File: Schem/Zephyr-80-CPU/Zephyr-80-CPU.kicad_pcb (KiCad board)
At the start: 6 copper layers, 160 x 64.4 mm, 62 parts, among them J1 pBITzBus, SW1 SW_Coded_SH-7070, SW2 SW_Coded_SH-7070, SW3 SW_Coded_SH-7070, SW4 SW_Coded_SH-7070, SW5 SW_Coded_SH-7070, SW6 SW_Coded_SH-7070, SW7 SW_Coded_SH-7070, U1 AS7C4096A-12TCN, U10 74HC244, U11 74HC244, U12 74HC138, U2 ATF22V10C-10PU, U3 Z084000xP, U4 SST39SF040-70-4C-PHE, U5 ATF22V10C-10PU, U6 SN74HC273DWR, U7 SN74HC244DWR, U8 74HC244, U9 74HC244, Y1 ECS-2100AX-100

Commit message: Routed the CPU board. Removed the rotary switches decoder
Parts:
- removed C10, C11, C12, C13, C9: 100n, Capacitor_SMD:C_0603_1608Metric
- removed R1, R10, R11, R12, R13, R14, R15, R16, R17, R18, R19, R2, R20, R21, R22, R23, R24, R25, R26, R27, R28, R3, R4, R5, R6, R7, R8, R9: 4k7, Resistor_SMD:R_0603_1608Metric
- removed SW1, SW2, SW3, SW4, SW5, SW6, SW7: SW_Coded_SH-7070, Button_Switch_THT:Nidec_Copal_SH-7010C
- removed U10, U11, U8, U9: 74HC244, Package_SO:TSSOP-20_4.4x6.5mm_P0.65mm
- removed U12: 74HC138, Package_SO:SSOP-16_5.3x6.2mm_P0.65mm
- moved U7 382.2 mm to (187.5, 78.0), turned to 0 degrees
- moved C3 380.6 mm to (153.1, 53.0), turned to 0 degrees
- moved C1 378.4 mm to (149.2, 53.0), turned to 180 degrees
- moved U6 376.2 mm to (187.5, 61.2), turned to 0 degrees
- moved C8 360.4 mm to (192.6, 69.6)
- moved C2 352.3 mm to (178.9, 53.1), turned to 180 degrees
- moved C4 345.5 mm to (192.1, 53.5), turned to 180 degrees
- moved C7 341.5 mm to (214.4, 87.5), turned to -90 degrees
- moved C5 328.9 mm to (212.3, 54.7), turned to 0 degrees
- moved C6 323.7 mm to (230.2, 87.4)
- moved U1 45.1 mm to (222.2, 87.0)
- moved U4 34.5 mm to (195.5, 56.9)
- moved U3 32.9 mm to (152.9, 55.8)
- moved Y1 24.1 mm to (133.2, 61.0)
- moved U5 20.9 mm to (171.5, 55.8)
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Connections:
- J1 pad A21: /Device Select Decode/~{CS2} -> /CPU and Address Decoding/CS_SEL2
- J1 pad A22: /Device Select Decode/~{CS3} -> unconnected-(J1A-CS3-PadA22)
- J1 pad B21: /Device Select Decode/~{CS0} -> /CPU and Address Decoding/CS_SEL0
- J1 pad B22: /Device Select Decode/~{CS1} -> /CPU and Address Decoding/CS_SEL1
- U1 pad 10: /CPU and Address Decoding/D1 -> /CPU and Address Decoding/D2
- U1 pad 13: /CPU and Address Decoding/D2 -> /CPU and Address Decoding/D0
- U1 pad 14: /CPU and Address Decoding/D3 -> /CPU and Address Decoding/D1
- U1 pad 3: /CPU and Address Decoding/A0 -> /CPU and Address Decoding/A1
- U1 pad 36: /CPU and Address Decoding/D7 -> /CPU and Address Decoding/D3
- U1 pad 4: /CPU and Address Decoding/A1 -> /CPU and Address Decoding/A0
- U1 pad 9: /CPU and Address Decoding/D0 -> /CPU and Address Decoding/D7
- U2 pad 16: /CPU and Address Decoding/~{IO_EN} -> unconnected-(U2-IO16-Pad16)
- U2 pad 7: /CPU and Address Decoding/~{RD} -> /CPU and Address Decoding/~{WR}
- U2 pad 8: /CPU and Address Decoding/~{WR} -> /CPU and Address Decoding/~{RD}
- U5 pad 1: /CPU and Address Decoding/A15 -> /CPU and Address Decoding/A13
- U5 pad 10: /CPU and Address Decoding/~{WR} -> /CPU and Address Decoding/~{RD}
- U5 pad 3: /CPU and Address Decoding/A13 -> /CPU and Address Decoding/A15
- U5 pad 9: /CPU and Address Decoding/~{RD} -> /CPU and Address Decoding/~{WR}
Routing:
- net /CPU and Address Decoding/A7: track 9.15 -> 202.8 mm, vias 0 -> 7
- net /CPU and Address Decoding/~{RD}: track 13.8 -> 197.4 mm, vias 0 -> 3
- net /CPU and Address Decoding/A8: track 0.00 -> 169.6 mm, vias 0 -> 6
- net /CPU and Address Decoding/A6: track 9.15 -> 176.6 mm, vias 0 -> 5
- net /CPU and Address Decoding/~{WR}: track 48.5 -> 215.5 mm, vias 1 -> 4
- net /CPU and Address Decoding/A5: track 9.15 -> 170.5 mm, vias 0 -> 5
- net /CPU and Address Decoding/A9: track 0.00 -> 160.8 mm, vias 0 -> 6
- net /CPU and Address Decoding/A10: track 0.00 -> 154.6 mm, vias 0 -> 5
- net /CPU and Address Decoding/A12: track 44.6 -> 188.7 mm, vias 1 -> 4
- net /CPU and Address Decoding/A4: track 9.15 -> 147.8 mm, vias 0 -> 5
- net GND: track 0.00 -> 133.3 mm, vias 0 -> 18
- net /CPU and Address Decoding/A2: track 0.00 -> 105.7 mm, vias 0 -> 5
- net /CPU and Address Decoding/A3: track 0.00 -> 105.2 mm, vias 0 -> 4
- net /CPU and Address Decoding/~{RESET}: track 16.8 -> 121.0 mm, vias 0 -> 4
- net /CPU and Address Decoding/A11: track 75.7 -> 175.8 mm, vias 1 -> 5
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- added copper zone on In2.Cu, net +5V
- added copper zone on In1.Cu, net GND

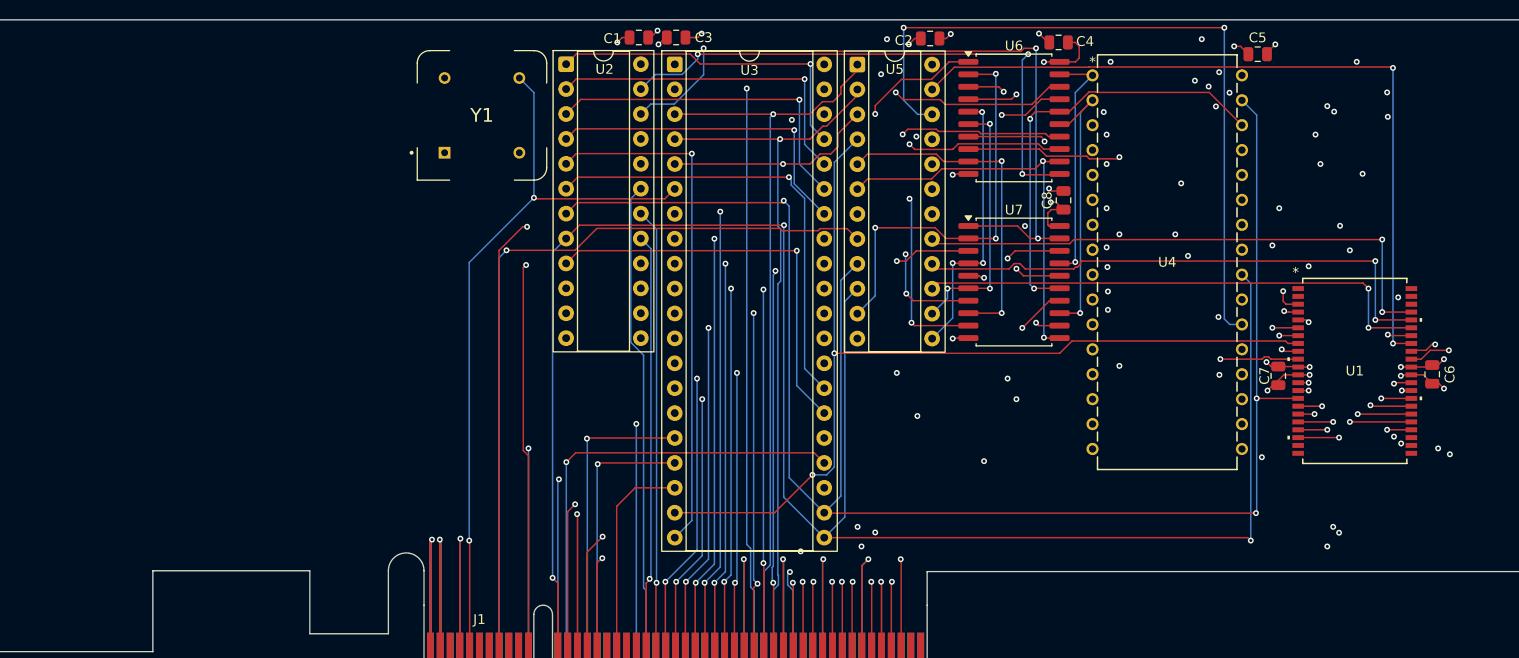
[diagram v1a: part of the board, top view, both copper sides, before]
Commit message: Added all the manufacturer part numbers to the KiCad schematics and PCB files. This will make it easier to order the parts for the project and ensure that the correct components are used. I also removed some of the old schematics that were no longer needed, such as the BaudClock, ConsolePort, DeviceSelectDecode, GPIOUserSerial, IO Controller, UserPorts, Video, and Z80HomeBrew schematics. These changes will help to streamline the design and make it easier to understand.
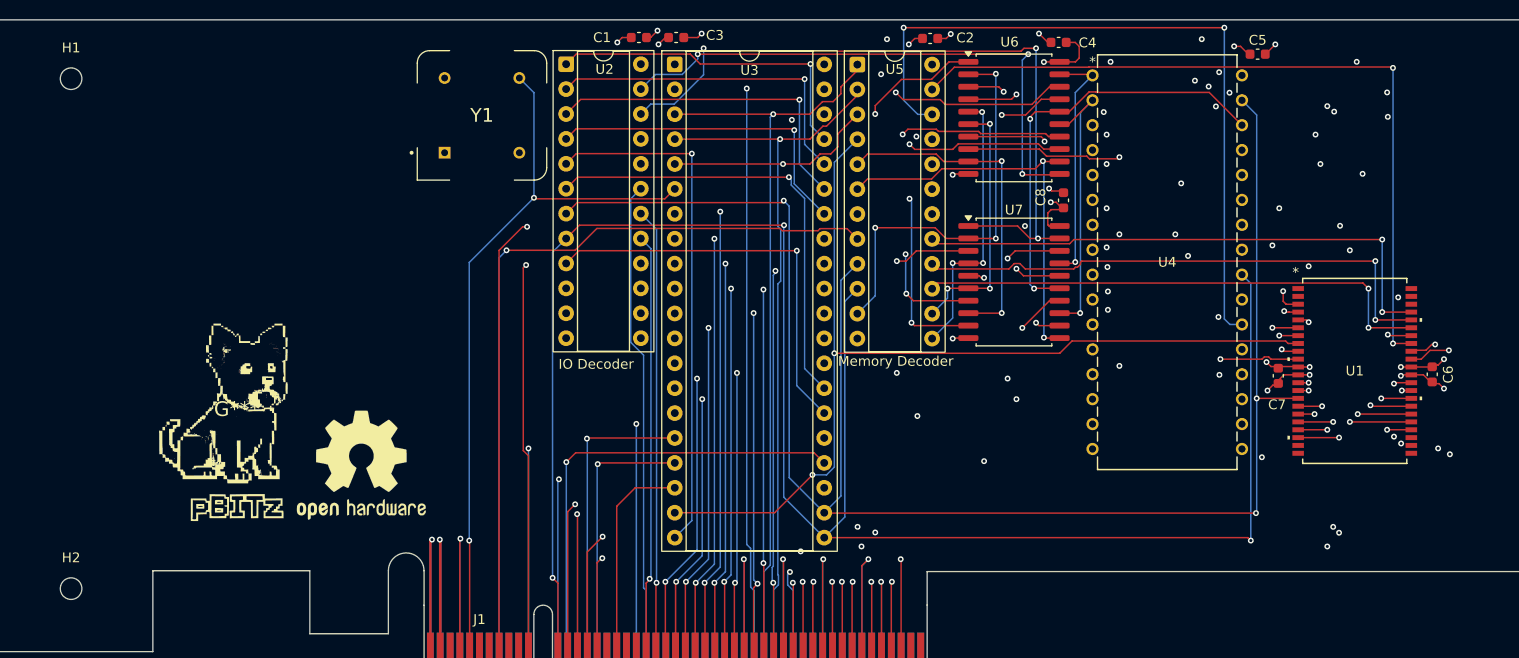
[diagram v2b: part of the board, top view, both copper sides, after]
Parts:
- added G***: LOGO, Footprints:pBITzlogo-Silk, F.Cu at (108.2, 90.9)
- added H1: MountingHole, MountingHole:MountingHole_2.2mm_M2, F.Cu at (91.3, 57.2)
- added H2: MountingHole, MountingHole:MountingHole_2.2mm_M2, F.Cu at (91.3, 109.2)
- added REF**: OSHW-Logo2_14.6x12mm_SilkScreen, Symbol:OSHW-Logo2_14.6x12mm_SilkScreen, F.Cu at (121.0, 96.6)
- C1, C2, C3, C4, C5, C6, C7, C8: footprint Capacitor_SMD:C_0805_2012Metric -> Capacitor_SMD:C_0603_1608Metric
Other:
- board text added: "IO Decoder"
- board text added: "Memory Decoder"

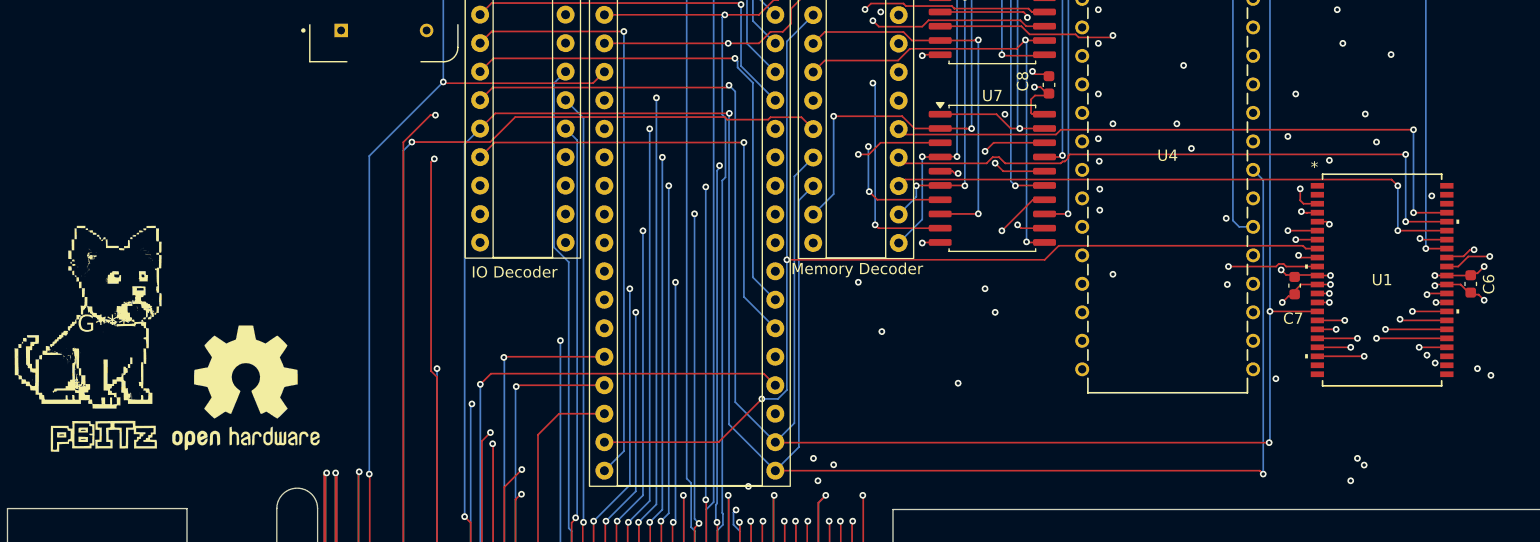
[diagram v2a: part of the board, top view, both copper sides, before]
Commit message: Fixed memory select wiring and added bulk cap on the power input.
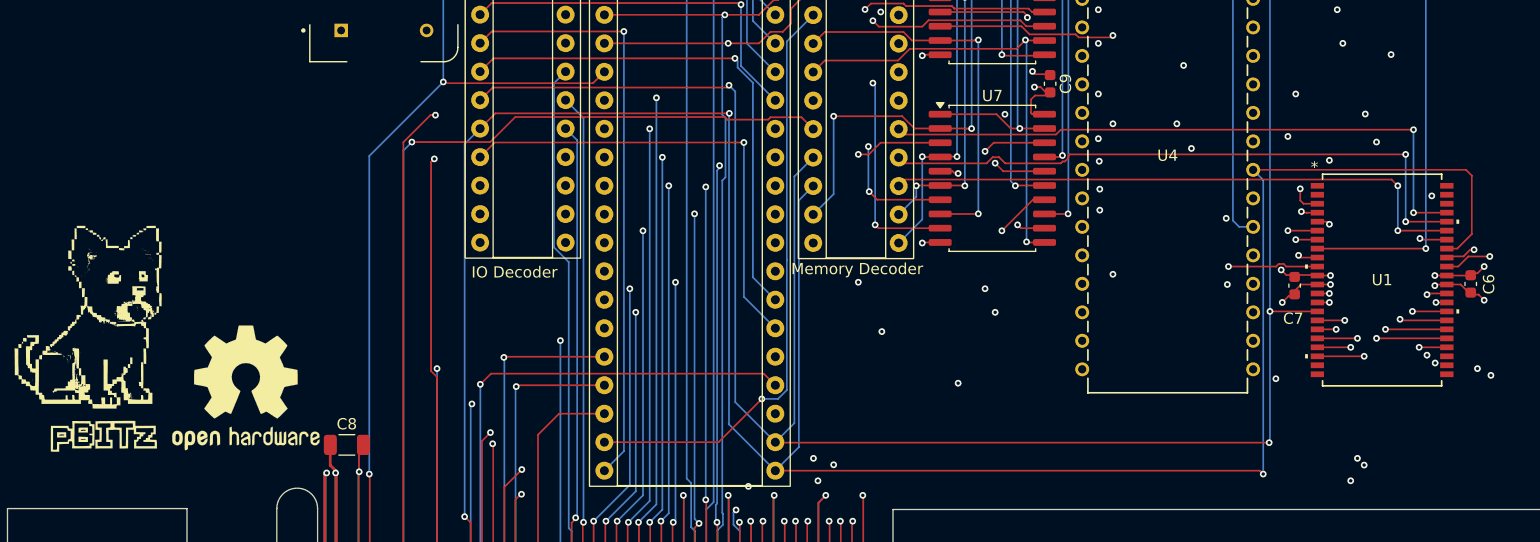
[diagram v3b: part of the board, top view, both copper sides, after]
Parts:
- added C9: 100n, Capacitor_SMD:C_0603_1608Metric, F.Cu at (192.7, 69.5)
- C8: value 100n -> 47u; footprint Capacitor_SMD:C_0603_1608Metric -> Capacitor_SMD:C_1206_3216Metric
- moved C8 70.4 mm to (129.9, 101.7), turned to 0 degrees
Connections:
- U1 pad 37: /CPU and Address Decoding/~{SRAM_CS} -> /CPU and Address Decoding/~{RD}
- U1 pad 8: /CPU and Address Decoding/~{MREQ} -> /CPU and Address Decoding/~{SRAM_CS}
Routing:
- net /CPU and Address Decoding/~{MREQ}: track 124.8 -> 76.9 mm, vias 3 -> 2
- net /CPU and Address Decoding/~{RD}: track 197.4 -> 225.1 mm
- net /CPU and Address Decoding/~{SRAM_CS}: track 78.0 -> 85.8 mm
- net +5V: track 73.4 -> 76.5 mm
- net GND: track 133.3 -> 135.8 mm

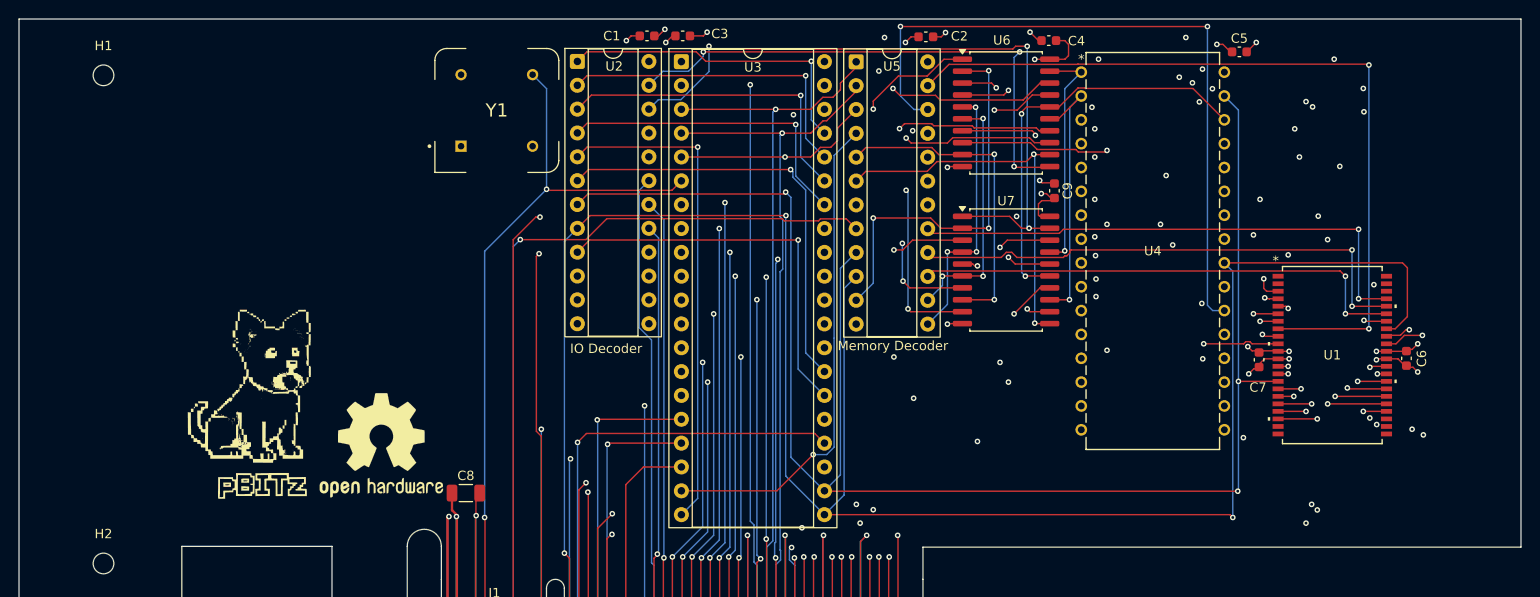
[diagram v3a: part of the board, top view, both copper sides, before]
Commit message: Added copper pours on top and bottom layers of IO controller board, and added a few vias to connect them. This should help with heat dissipation and EMI shielding.
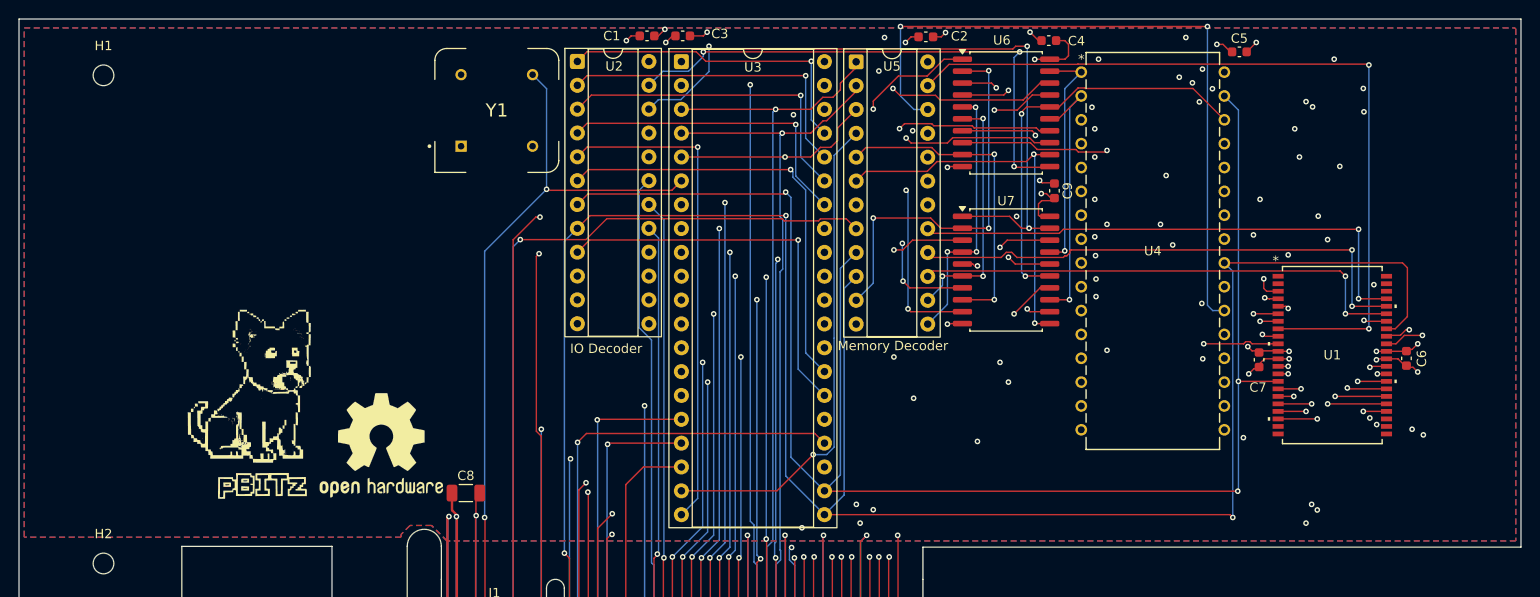
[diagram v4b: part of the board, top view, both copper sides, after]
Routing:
- added copper zone on B.Cu, net GND
- added copper zone on F.Cu, net GND
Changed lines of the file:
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@@
+		(net 1)
+		(net_name "GND")
+		(layers "F.Cu" "B.Cu")
+		(hatch edge 0.5)
+		(priority 2)
+		(connect_pads no
+			(clearance 0.4)
+		)
+		(min_thickness 0.127)
+		(filled_areas_thickness no)
+		(fill yes
+			(thermal_gap 0.254)
+			(thermal_bridge_width 0.254)
+			(smoothing chamfer)
+		)
+		(polygon
+			(pts
+				(xy 241.7 52.17) (xy 241.8 52.27) (xy 241.8 106.82) (xy 127.95 106.82) (xy 126.3 105.17) (xy 124 105.17)
+				(xy 123.05 106.12) (xy 123.05 106.42) (xy 82.95 106.42) (xy 82.9 106.37) (xy 82.9 52.17)
+			)
+		)
+	)
+	(zone
 		(net 1)
 		(net_name "GND")
